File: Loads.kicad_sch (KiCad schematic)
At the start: 1 part

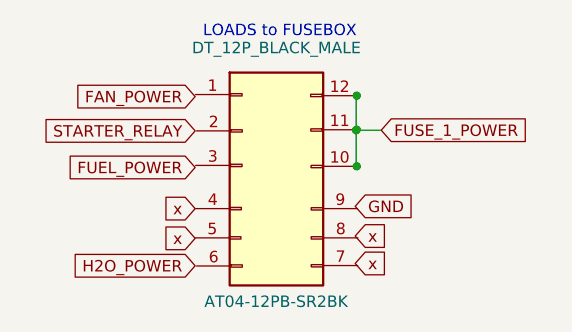
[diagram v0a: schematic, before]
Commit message: readd all connectors
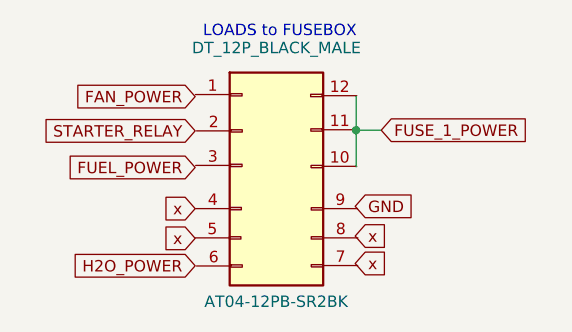
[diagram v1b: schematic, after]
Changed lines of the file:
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@@
-(kicad_sch (version 20211123) (generator eeschema)
+(kicad_sch (version 20230121) (generator eeschema)
   (paper "A4")
-  (junction (at 118.7958 64.389) (diameter 0) (color 0 0 0 0)
-  )
-  (junction (at 118.7958 68.453) (diameter 0) (color 0 0 0 0)
-  )
-  (junction (at 118.7958 60.6044) (diameter 0) (color 0 0 0 0)
-  )
   (junction (at 118.7196 64.4398) (diameter 0) (color 0 0 0 0)
   )
   (wire (pts (xy 121.5136 64.4398) (xy 118.7196 64.4398))
-    (stroke (width 0) (type default) (color 0 0 0 0))
+    (stroke (width 0) (type default))
   )
   (wire (pts (xy 118.7196 64.4398) (xy 118.7196 68.5038))
-    (stroke (width 0) (type default) (color 0 0 0 0))
+    (stroke (width 0) (type default))
   )
   (wire (pts (xy 118.7196 60.6298) (xy 118.7196 64.4398))
-    (stroke (width 0) (type default) (color 0 0 0 0))
+    (stroke (width 0) (type default))
   )
   (text "LOADS to FUSEBOX" (at 101.7016 54.2798 0)
@@
   (global_label "x" (shape input) (at 100.838 73.152 180) (fields_autoplaced)
     (effects (font (size 1.27 1.27)) (justify right))
-    (property "Intersheet References" "${INTERSHEET_REFS}" (id 0) (at 97.3968 73.0726 0)
+    (property "Intersheetrefs" "${INTERSHEET_REFS}" (at 97.3968 73.0726 0)
       (effects (font (size 1.27 1.27)) (justify right) hide)
     )
@@
   (global_label "STARTER_RELAY" (shape input) (at 100.838 64.516 180) (fields_autoplaced)
     (effects (font (size 1.27 1.27)) (justify right))
-    (property "Intersheet References" "${INTERSHEET_REFS}" (id 0) (at 83.9106 64.4366 0)
+    (property "Intersheetrefs" "${INTERSHEET_REFS}" (at 83.9106 64.4366 0)
       (effects (font (size 1.27 1.27)) (justify right) hide)
     )
@@
   (global_label "GND" (shape input) (at 118.618 72.898 0) (fields_autoplaced)
     (effects (font (size 1.27 1.27)) (justify left))
-    (property "Intersheet References" "${INTERSHEET_REFS}" (id 0) (at 124.9016 72.8186 0)
+    (property "Intersheetrefs" "${INTERSHEET_REFS}" (at 124.9016 72.8186 0)
       (effects (font (size 1.27 1.27)) (justify left) hide)
     )
@@
   (global_label "FUSE_1_POWER" (shape input) (at 121.5136 64.4398 0) (fields_autoplaced)
     (effects (font (size 1.27 1.27)) (justify left))
-    (property "Intersheet References" "${INTERSHEET_REFS}" (id 0) (at 138.32 64.3604 0)
+    (property "Intersheetrefs" "${INTERSHEET_REFS}" (at 138.32 64.3604 0)
       (effects (font (size 1.27 1.27)) (justify left) hide)
     )
@@
   (global_label "FAN_POWER" (shape input) (at 100.838 60.706 180) (fields_autoplaced)
     (effects (font (size 1.27 1.27)) (justify right))
-    (property "Intersheet References" "${INTERSHEET_REFS}" (id 0) (at 87.4787 60.6266 0)
+    (property "Intersheetrefs" "${INTERSHEET_REFS}" (at 87.4787 60.6266 0)
       (effects (font (size 1.27 1.27)) (justify right) hide)
     )
@@
   (global_label "x" (shape input) (at 100.838 76.454 180) (fields_autoplaced)
     (effects (font (size 1.27 1.27)) (justify right))
-    (property "Intersheet References" "${INTERSHEET_REFS}" (id 0) (at 97.3968 76.3746 0)
+    (property "Intersheetrefs" "${INTERSHEET_REFS}" (at 97.3968 76.3746 0)
       (effects (font (size 1.27 1.27)) (justify right) hide)
     )
@@
   (global_label "x" (shape input) (at 118.618 79.248 0) (fields_autoplaced)
     (effects (font (size 1.27 1.27)) (justify left))
-    (property "Intersheet References" "${INTERSHEET_REFS}" (id 0) (at 122.0592 79.1686 0)
+    (property "Intersheetrefs" "${INTERSHEET_REFS}" (at 122.0592 79.1686 0)
       (effects (font (size 1.27 1.27)) (justify left) hide)
     )
@@
   (global_label "x" (shape input) (at 118.618 76.2 0) (fields_autoplaced)
     (effects (font (size 1.27 1.27)) (justify left))
-    (property "Intersheet References" "${INTERSHEET_REFS}" (id 0) (at 122.0592 76.1206 0)
+    (property "Intersheetrefs" "${INTERSHEET_REFS}" (at 122.0592 76.1206 0)
       (effects (font (size 1.27 1.27)) (justify left) hide)
     )
@@
   (global_label "H2O_POWER" (shape input) (at 100.838 79.502 180) (fields_autoplaced)
     (effects (font (size 1.27 1.27)) (justify right))
-    (property "Intersheet References" "${INTERSHEET_REFS}" (id 0) (at 87.1159 79.4226 0)
+    (property "Intersheetrefs" "${INTERSHEET_REFS}" (at 87.1159 79.4226 0)
       (effects (font (size 1.27 1.27)) (justify right) hide)
     )
@@
   (global_label "FUEL_POWER" (shape input) (at 100.838 68.58 180) (fields_autoplaced)
     (effects (font (size 1.27 1.27)) (justify right))
-    (property "Intersheet References" "${INTERSHEET_REFS}" (id 0) (at 86.3901 68.5006 0)
+    (property "Intersheetrefs" "${INTERSHEET_REFS}" (at 86.3901 68.5006 0)
       (effects (font (size 1.27 1.27)) (justify right) hide)
     )
   )
   (symbol (lib_id "SCR23 Library:DTM04-12pb") (at 109.5756 70.7898 0) (unit 1)
-    (in_bom yes) (on_board yes)
-    (property "Reference" "U?" (id 0) (at 109.8677 53.0098 0)
+    (in_bom yes) (on_board yes) (dnp no)
+    (property "Reference" "U?" (at 109.8677 53.0098 0)
       (effects (font (size 1.27 1.27)) hide)
     )
-    (property "Value" "DT_12P_BLACK_MALE" (id 1) (at 109.8677 55.2958 0))
-    (property "Footprint" "" (id 2) (at 109.5756 80.9498 0)
+    (property "Value" "DT_12P_BLACK_MALE" (at 109.8677 55.2958 0)
+      (effects (font (size 1.27 1.27)))
+    )
+    (property "Footprint" "" (at 109.5756 80.9498 0)
       (effects (font (size 1.27 1.27)) hide)
     )
-    (property "Datasheet" "" (id 3) (at 109.5756 80.9498 0)
+    (property "Datasheet" "" (at 109.5756 80.9498 0)
       (effects (font (size 1.27 1.27)) hide)
     )
-    (property "Part #" "AT04-12PB-SR2BK" (id 4) (at 109.8296 83.4898 0))
+    (property "Part #" "AT04-12PB-SR2BK" (at 109.8296 83.4898 0)
+      (effects (font (size 1.27 1.27)))
+    )
     (pin "1")
     (pin "10")
@@
     (pin "8")
     (pin "9")
+    (instances
+      (project "F22 V2 Wiring Schematic"
+        (path "/64503d07-5f6a-4ffd-b005-97f9848c9cbf/c61ebb53-a6d0-4444-86d9-f19c0fecfdba/6d55809a-8068-448f-a4a2-c0051f118b1f"
+          (reference "U?") (unit 1)
+        )
+      )
+    )
   )
 )

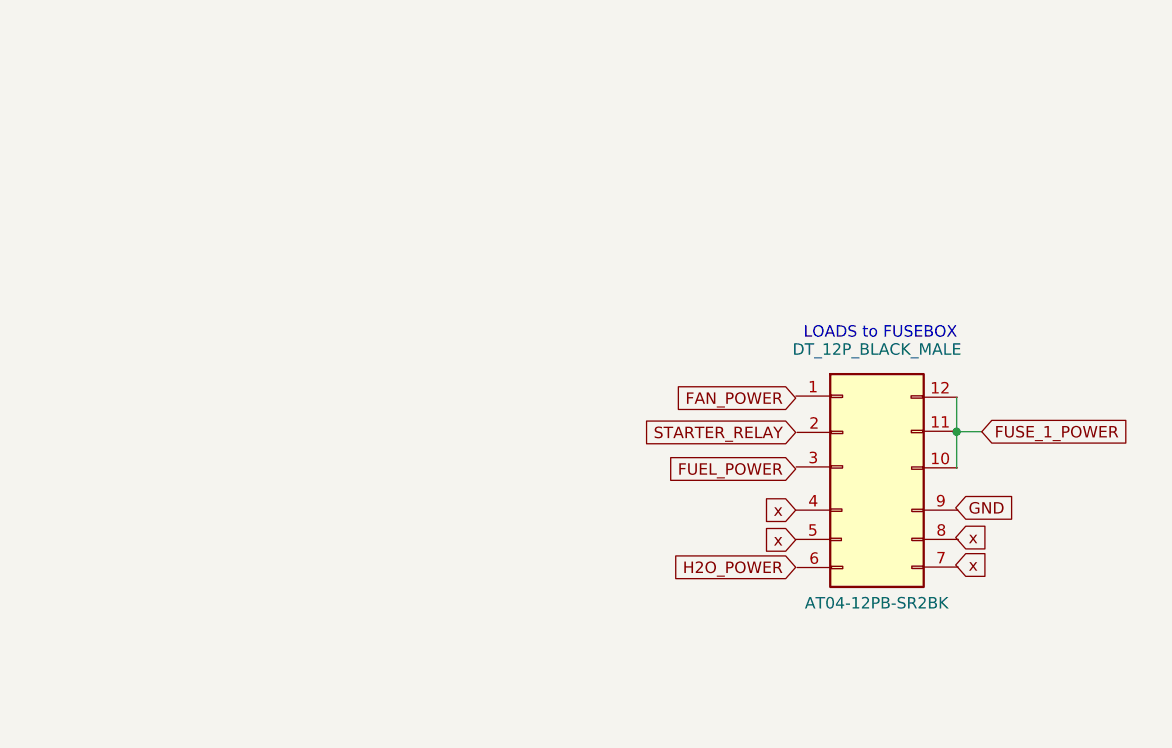
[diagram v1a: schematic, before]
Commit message: Updating Connectors
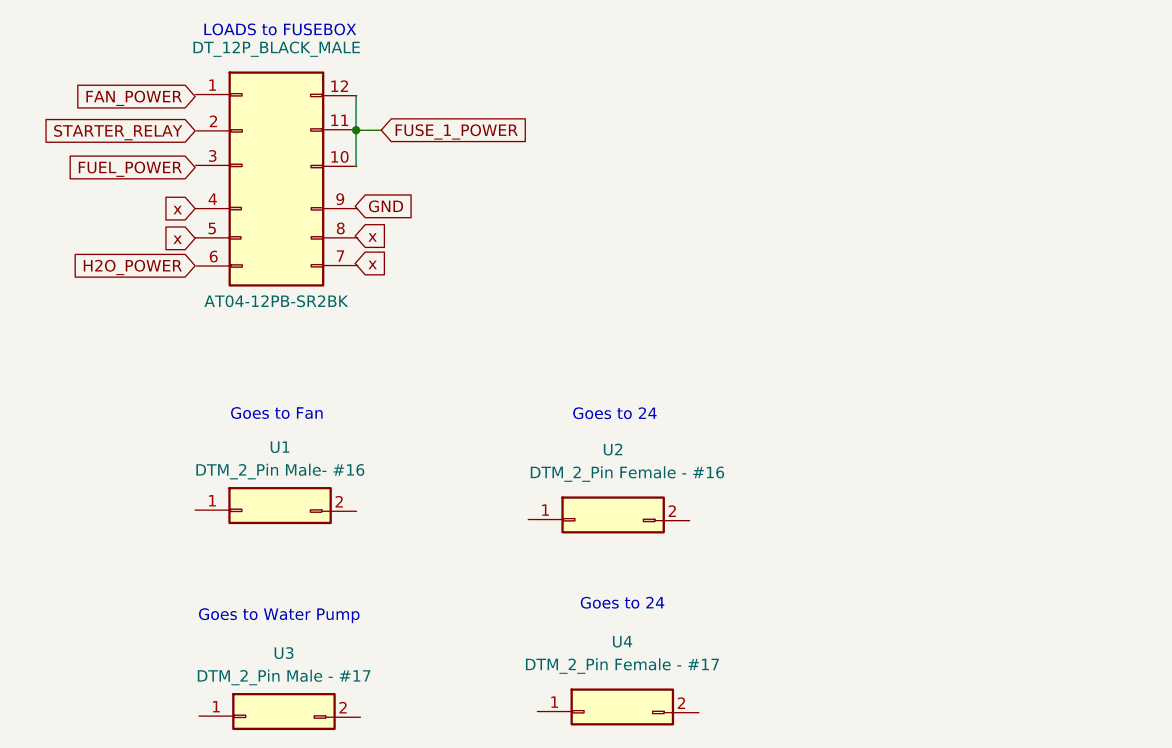
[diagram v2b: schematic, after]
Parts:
- added U1: DTM_2_Pin Male- #16, symbol SCR23 Library:DTM_2_Pin
- added U2: DTM_2_Pin Female - #16, symbol SCR23 Library:DTM_2_Pin
- added U3: DTM_2_Pin Male - #17, symbol SCR23 Library:DTM_2_Pin
- added U4: DTM_2_Pin Female - #17, symbol SCR23 Library:DTM_2_Pin
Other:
- note added: "Goes to 24"
- note added: "Goes to Fan"
- note added: "Goes to Water Pump"
